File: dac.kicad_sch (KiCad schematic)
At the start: 16 parts, among them J9 DAC OUT, U1 CJC4334H

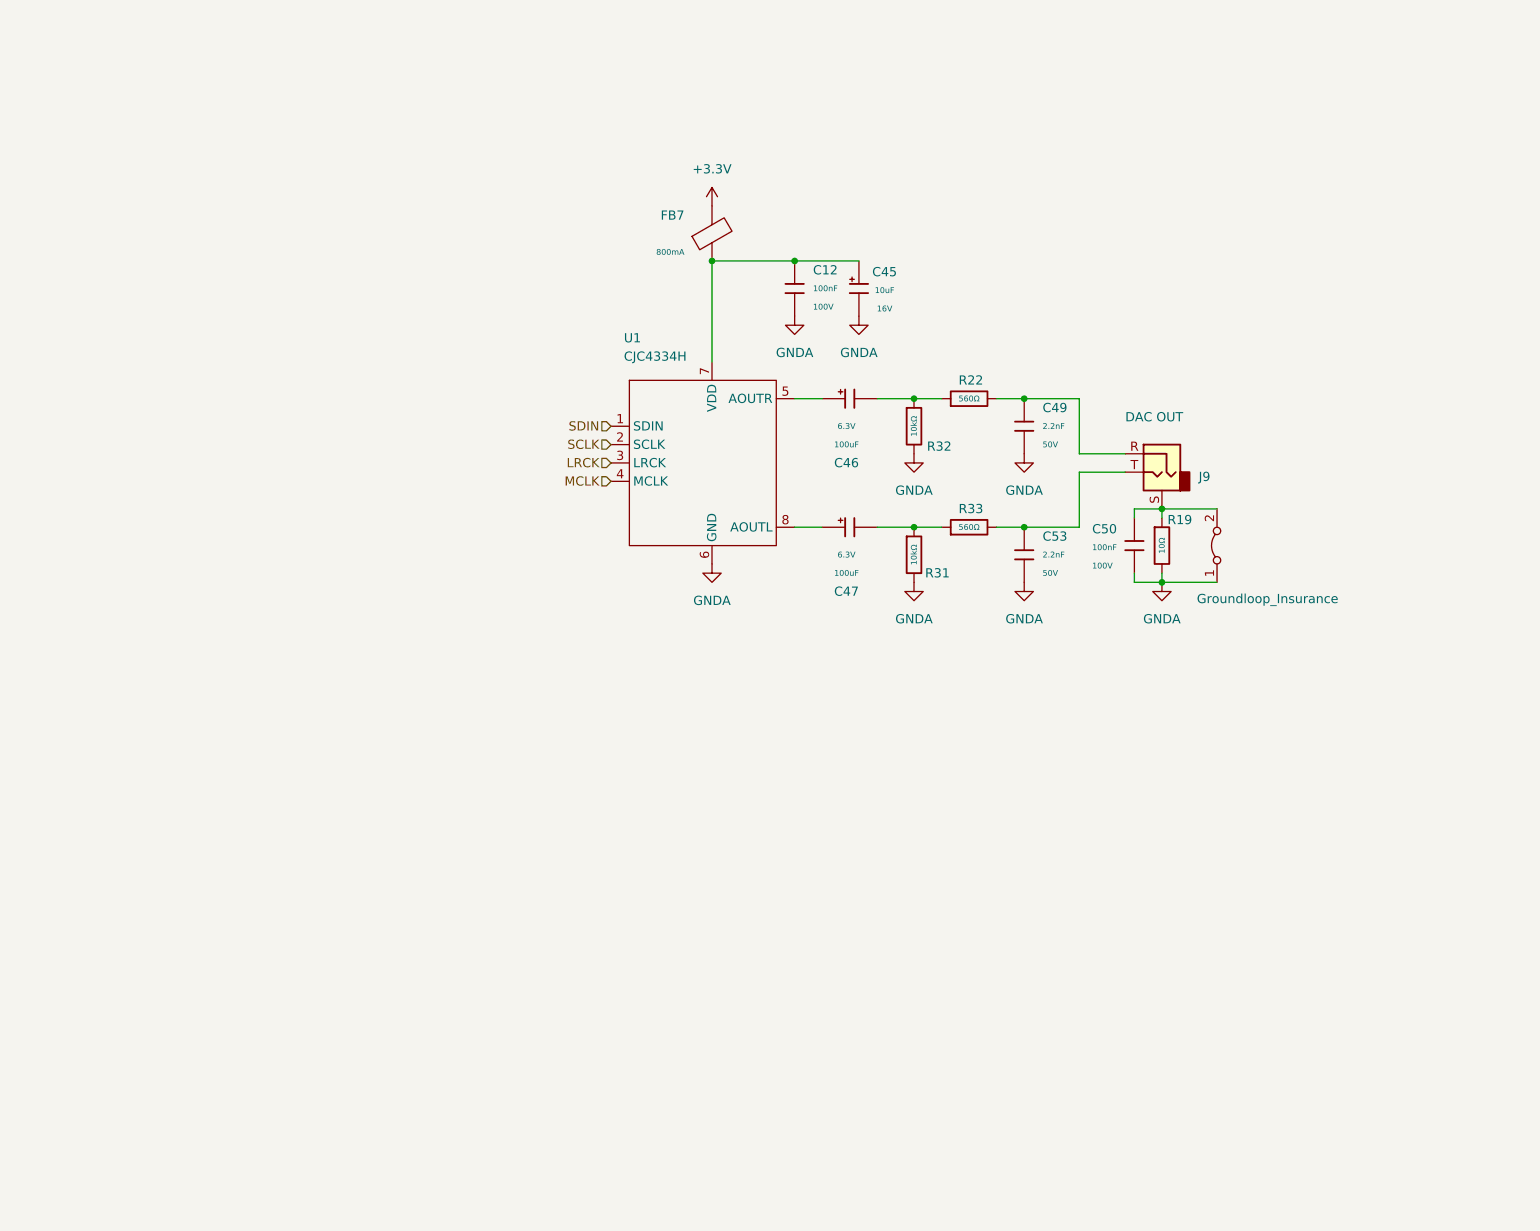
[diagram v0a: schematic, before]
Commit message: Added DAC Amp for Paula and Shaina.
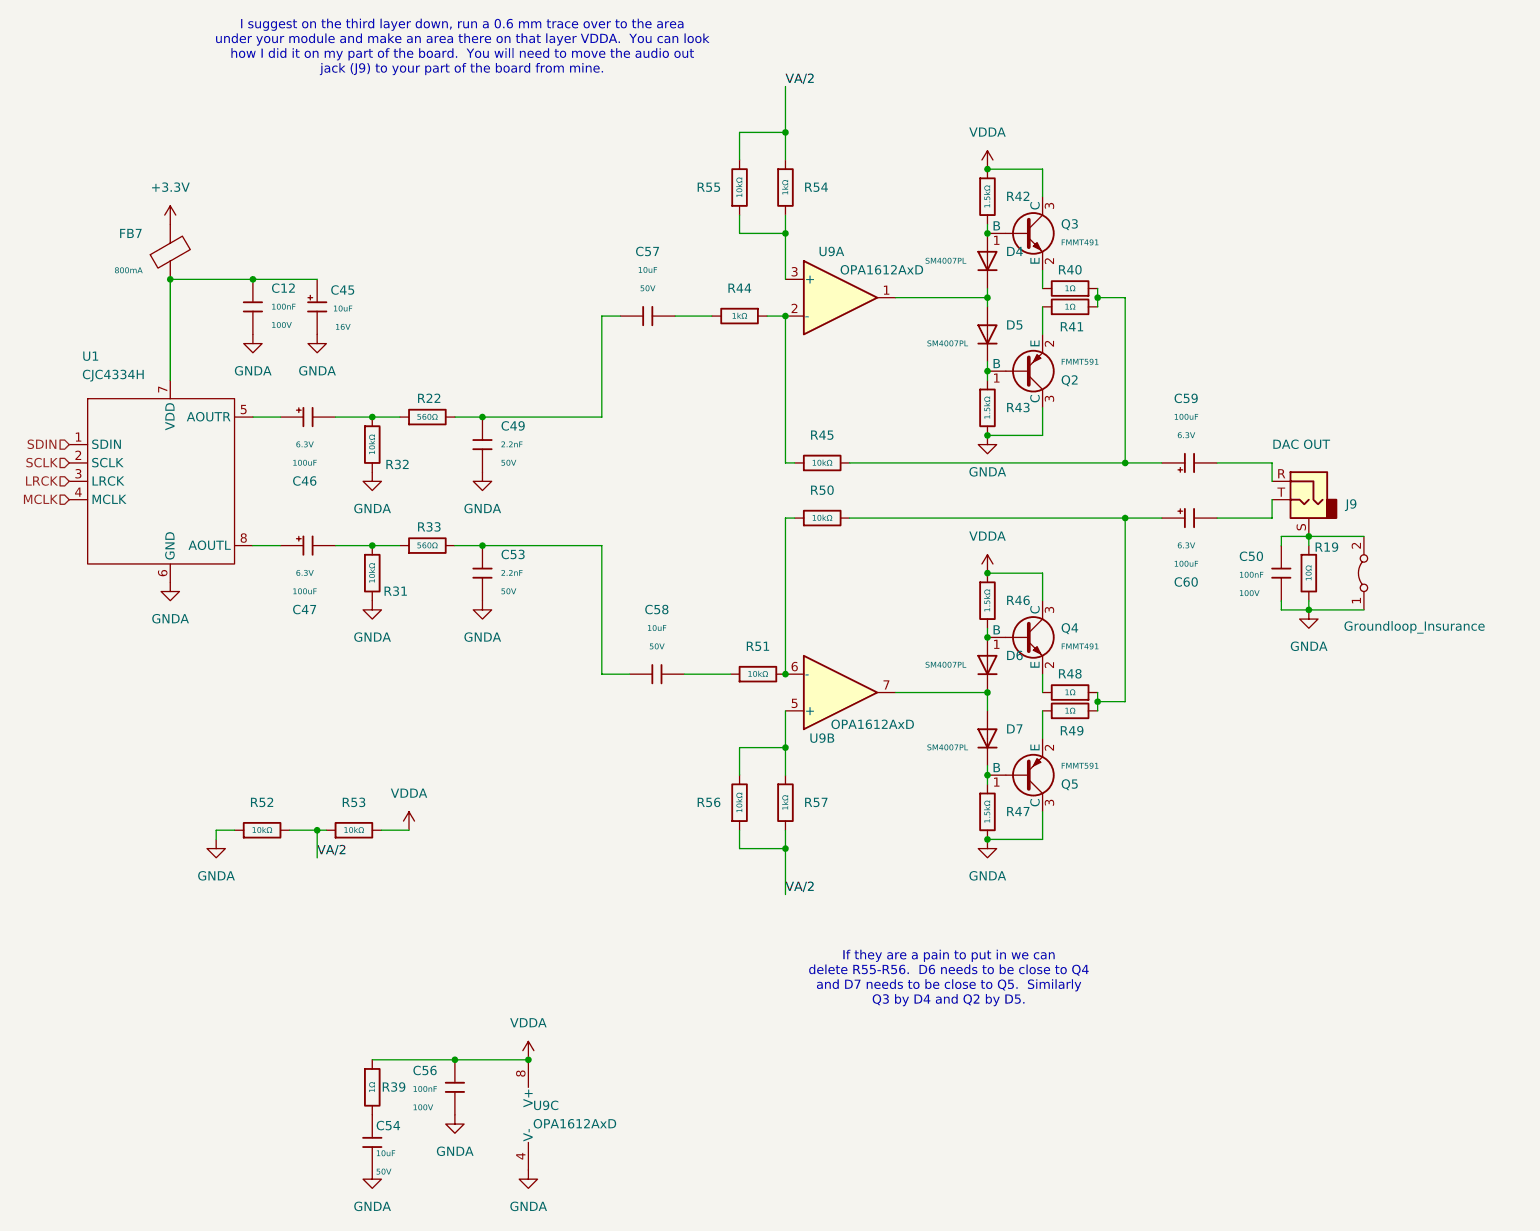
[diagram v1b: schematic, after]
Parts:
- added C54: 10uF, PCM_JLCPCB:C_1206, symbol PCM_JLCPCB-Capacitors:1206,10uF
- added C56: 100nF, PCM_JLCPCB:C_0805, symbol PCM_JLCPCB-Capacitors:0805,100nF
- added C57, C58: 10uF, PCM_JLCPCB:C_0805, symbol PCM_JLCPCB-Capacitors:0805,10uF,(2)
- added C59, C60: 100uF, PCM_JLCPCB:C_CASE-B-3528-21(mm), symbol PCM_JLCPCB-Capacitors:CASE-B-3528-21(mm),100uF
- added D4, D5, D6, D7: SM4007PL, PCM_JLCPCB:D_SOD-123FL, symbol PCM_JLCPCB-Diodes:General,SM4007PL
- added Q2, Q5: FMMT591, PCM_JLCPCB:Q_SOT-23, symbol PCM_JLCPCB-Transistors:PNP,FMMT591
- added Q3, Q4: FMMT491, PCM_JLCPCB:Q_SOT-23, symbol PCM_JLCPCB-Transistors:NPN,FMMT491
- added R39, R40, R41, R48, R49: 1Ω, PCM_JLCPCB:R_0805, symbol PCM_JLCPCB-Resistors:0805,1Ω
- added R42, R43, R46, R47: 1.5kΩ, PCM_JLCPCB:R_0805, symbol PCM_JLCPCB-Resistors:0805,1.5kΩ
- added R44, R54, R57: 1kΩ, PCM_JLCPCB:R_0805, symbol PCM_JLCPCB-Resistors:0805,1kΩ
- added R45, R50, R51, R52, R53, R55, R56: 10kΩ, PCM_JLCPCB:R_0805, symbol PCM_JLCPCB-Resistors:0805,10kΩ
- added U9: OPA1612AxD, Package_SO:SOIC-8_3.9x4.9mm_P1.27mm, symbol Amplifier_Operational:OPA1612AxD
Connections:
- net GNDA: now also C54.2, C56.1, Q2.3 (C), Q5.3 (C), R43.2, R47.2, R52.1, U9.4 (V-)
- net at C49.1, R22.2: now also C57.1; no longer J9.R
- net at C53.1, R33.2: now also C58.1; no longer J9.T
- new net: C60.1, R48.1, R49.2, R50.2
- new net: C60.2, J9.T
- new net: Q5.2 (E), R49.1
- new net: R44.1, R45.1, U9.2 (-)
- new net: C57.2, R44.2
- new net: C59.2, J9.R
- new net: D4.1, D5.2, U9.1
- new net: R54.2, R55.1, U9.3 (+)
- new net: C58.2, R51.1
- new net: D5.1, Q2.1 (B), R43.1
- new net: D6.1, D7.2, U9.7
- new net: D6.2, Q4.1 (B), R46.2
- new net: C54.1, R39.2
- new net: D7.1, Q5.1 (B), R47.1
- new net: C59.1, R40.1, R41.2, R45.2
- new net: R56.2, R57.1, U9.5 (+)
- new net: R50.1, R51.2, U9.6 (-)
- new net: Q2.2 (E), R41.1
- new net: Q4.2 (E), R48.2
- new net: Q3.2 (E), R40.2
- new net: D4.2, Q3.1 (B), R42.2
- new net VA/2: R52.2, R53.1, R54.1, R55.2, R56.1, R57.2
- new net VDDA: C56.2, Q3.3 (C), Q4.3 (C), R39.1, R42.1, R46.1, R53.2, U9.8 (V+)
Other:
- note added: "I suggest on the third layer down, run a 0.6 mm trace over to the area under your module and make an area there on that layer VDDA. You can look how I did it on my part of the board. You will need to move the audio out jack (J9) to your part of the board from mine."
- note added: "If they are a pain to put in we can delete R55-R56. D6 needs to be close to Q4 and D7 needs to be close to Q5. Similarly Q3 by D4 and Q2 by D5."
- moved on the sheet: C12, C45, C46, C47, C49, C50, C53, FB7, J9, R19, R22, R31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
